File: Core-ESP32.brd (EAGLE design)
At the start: 106 x 100 mm, 74 parts, among them J3 CONNECTOR-GROVE-4P-2.0-347013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, Q1 BSS138, Q10 BSS138, Q11 BSS138, Q12 BSS138, Q13 BSS138, Q14 BSS138, Q15 BSS138, Q16 BSS138, Q17 BSS138, Q2 BSS138, Q3 BSS138, Q4 BSS138, Q5 BSS138, Q6 BSS138, Q7 BSS138, Q8 BSS138, Q9 BSS138

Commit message: cleanup
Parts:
- removed I2CLED1: (no value), SPCoast:1X04_LOCK
- removed J3: CONNECTOR-GROVE-4P-2.0-3470130P1, SPCoast:4P-2.0
- added LED1: G, SPCoast:0603-LED
- added PWROUT: CONNECTOR-POWER-R, SPCoast:POWER-R
- added R35: 2k2, SPCoast:0603-RES
- moved R26 6.10 mm to (77.7, 53.3)
- moved R27 5.97 mm to (82.9, 53.3)
- moved R29 5.97 mm to (88.0, 53.3)
- moved R25 5.84 mm to (72.9, 53.3)
- moved R24 5.72 mm to (67.9, 53.3)
- moved R22 5.08 mm to (58.4, 53.3)
- moved R23 4.95 mm to (63.6, 53.3)
- moved Q1 4.83 mm to (84.1, 49.7)
- moved Q14 4.83 mm to (89.2, 49.5)
- moved R14 4.83 mm to (84.1, 45.7)
- moved R28 4.83 mm to (89.2, 45.7)
- moved Q11 4.83 mm to (68.8, 49.5)
- moved Q12 4.83 mm to (73.9, 49.5)
- moved Q13 4.83 mm to (79.0, 49.5)
- moved R11 4.83 mm to (68.8, 45.7)
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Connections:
- new net N$1: LED1.A, R35.1
- net +3V3: no longer I2CLED1.3
- net +9V: now also PWROUT.V+, PWROUT.V+@1, PWROUT.V+@2, PWROUT.V+@3; no longer J3.3, J3.4
- net GND: now also LED1.C, PWROUT.GND, PWROUT.GND@1, PWROUT.GND@2, PWROUT.GND@3; no longer I2CLED1.4, J3.1, J3.2
- net SCL: no longer I2CLED1.2
- net SDA: no longer I2CLED1.1
- net VCCIO: now also R35.2
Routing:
- net SDA: track 79.9 -> 43.8 mm
- net VCCIO: track 312.7 -> 342.6 mm, vias 17 -> 20
- net N$1: track 0.00 -> 19.1 mm
- net +3V3: track 249.1 -> 234.7 mm, vias 21 -> 22
- net +9V: track 199.0 -> 211.1 mm
- net GND: track 18.8 -> 7.00 mm
- net SCL: track 51.5 -> 42.3 mm
- net D13: track 71.5 -> 62.7 mm
- net D27: track 58.5 -> 51.7 mm
- net D25H: track 41.8 -> 35.6 mm
- net D25: track 42.2 -> 36.1 mm
- net D14: track 53.3 -> 47.3 mm
- net D23H: track 40.1 -> 34.7 mm
- net D26H: track 47.5 -> 43.2 mm
- net SCLH: track 60.3 -> 64.4 mm
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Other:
- board text added: "128x32"
- board text added: "128x64"
- board text added: "3v3 I/O"
- board text removed: "+ -"
- board text removed: "128x32 -or- 128x64"

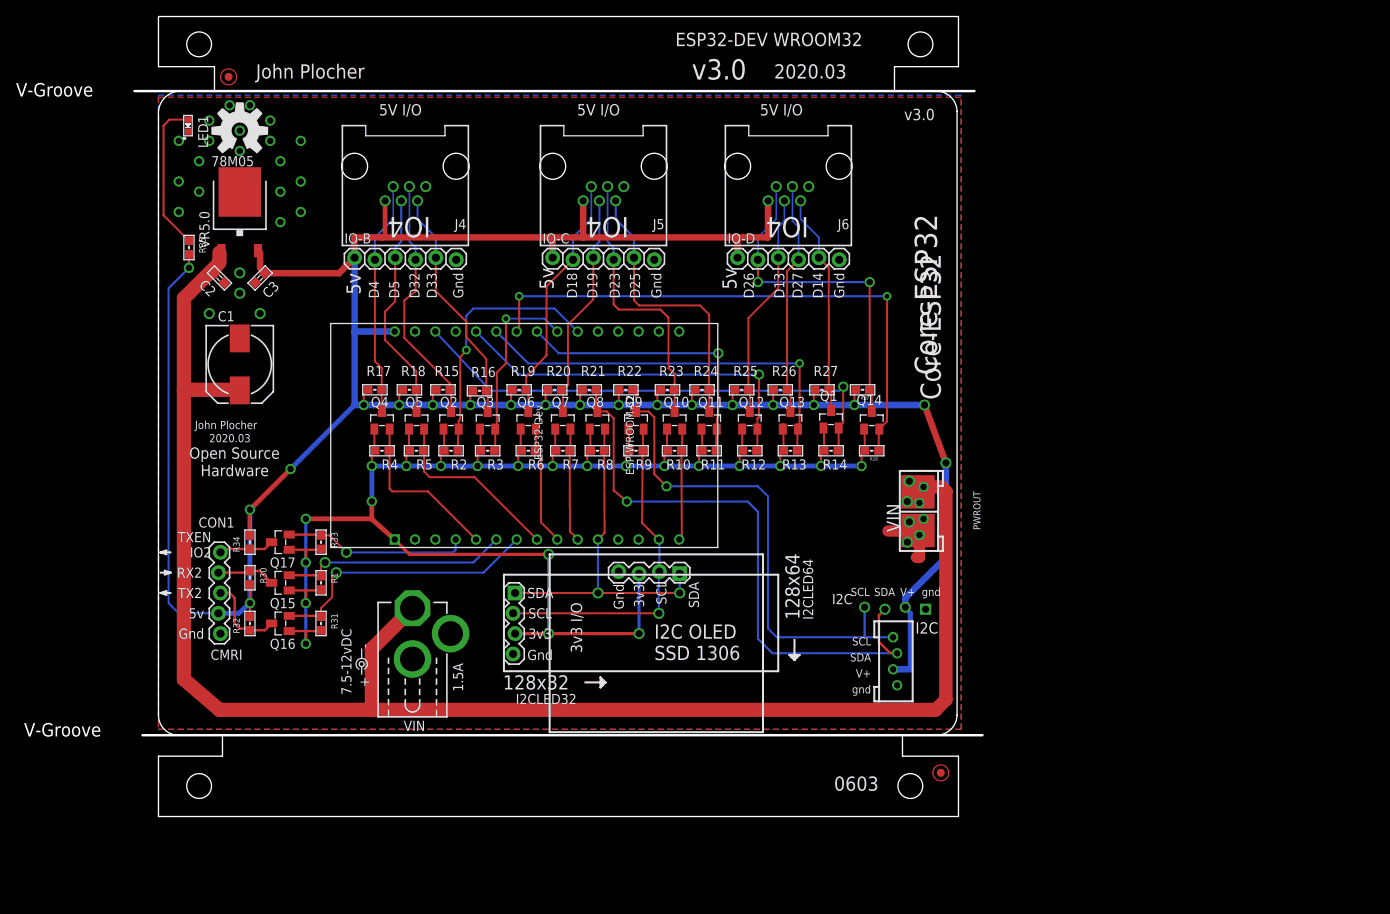
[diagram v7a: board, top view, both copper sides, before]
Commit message: convert to 30-pin DEV board, add CMRI-net IO
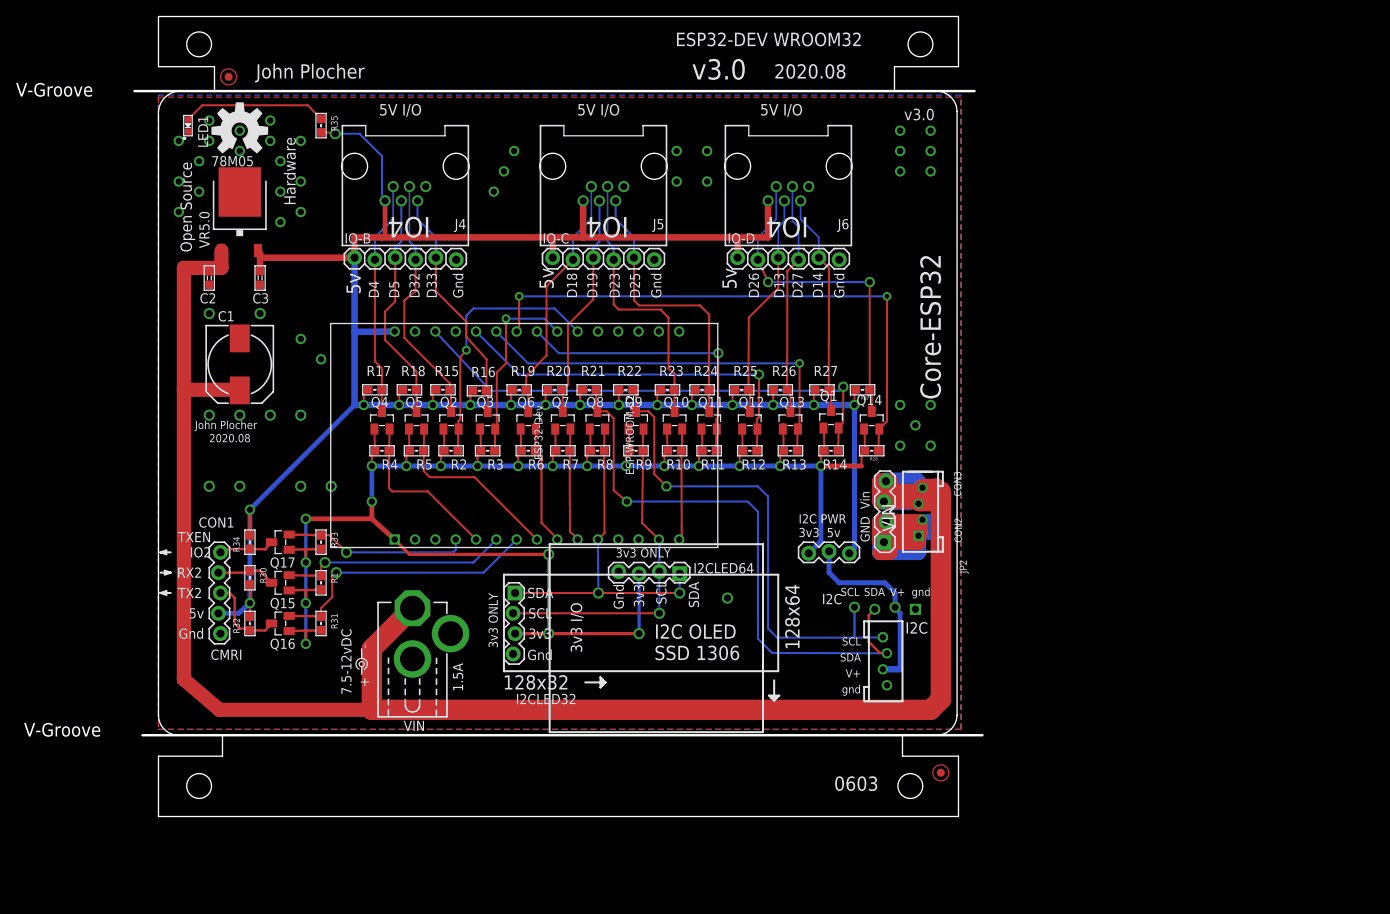
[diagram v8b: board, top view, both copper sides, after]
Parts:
- removed PWROUT: CONNECTOR-POWER-R, SPCoast:POWER-R
- added CON2: (no value), SPCoast:1X04_LOCK
- added CON3: (no value), SPCoast:4P-2.0
- added JP2: (no value), SPCoast:1X03
- moved R35 22.5 mm to (20.3, 86.4)
- moved C2 1.27 mm to (6.35, 67.3), turned to 270 degrees
- moved I2C 1.27 mm to (90.8, 26.0)
- turned C3 to 270 degrees
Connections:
- new net N$3: I2C.V+, I2C.V+@1, JP2.2
- net +3V3: now also JP2.1
- net +9V: now also CON2.3, CON2.4, CON3.3, CON3.4; no longer PWROUT.V+, PWROUT.V+@1, PWROUT.V+@2, PWROUT.V+@3
- net GND: now also CON2.1, CON2.2, CON3.1, CON3.2; no longer PWROUT.GND, PWROUT.GND@1, PWROUT.GND@2, PWROUT.GND@3
- net VCCIO: now also JP2.3; no longer I2C.V+, I2C.V+@1
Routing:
- net VCCIO: track 342.6 -> 276.8 mm, vias 20 -> 17
- net GND: track 7.00 -> 46.8 mm, vias 23 -> 48
- net +9V: track 211.1 -> 243.5 mm
- net N$3: track 0.00 -> 23.9 mm
- net +3V3: track 234.7 -> 246.3 mm, vias 22 -> 21
- net SDAH: track 74.7 -> 73.4 mm
- net SCLH: track 64.4 -> 63.2 mm
- net D26H: track 43.2 -> 42.2 mm
- net N$1: track 19.1 -> 18.1 mm
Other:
- board text added: "2020.08"
- board text added: "3v3 ONLY"
- board text added: "GND Vin"
- board text added: "I2C PWR 3v3 5v"
- board text removed: "2020.03"
- board text removed: "Core ESP32"
